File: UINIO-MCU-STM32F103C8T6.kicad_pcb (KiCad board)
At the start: 2 copper layers, 68.4 x 20.3 mm, 40 parts, among them J1 Conn_01x24_Pin, J2 Conn_01x24_Pin, J3 Conn_01x04_Pin, SW1 BOOT1, SW2 NRST, SW3 BOOT0, U1 ME6211C33M5G-N, U2 STM32F103C8T6, Y1 32.768KHz, Y2 8MHz

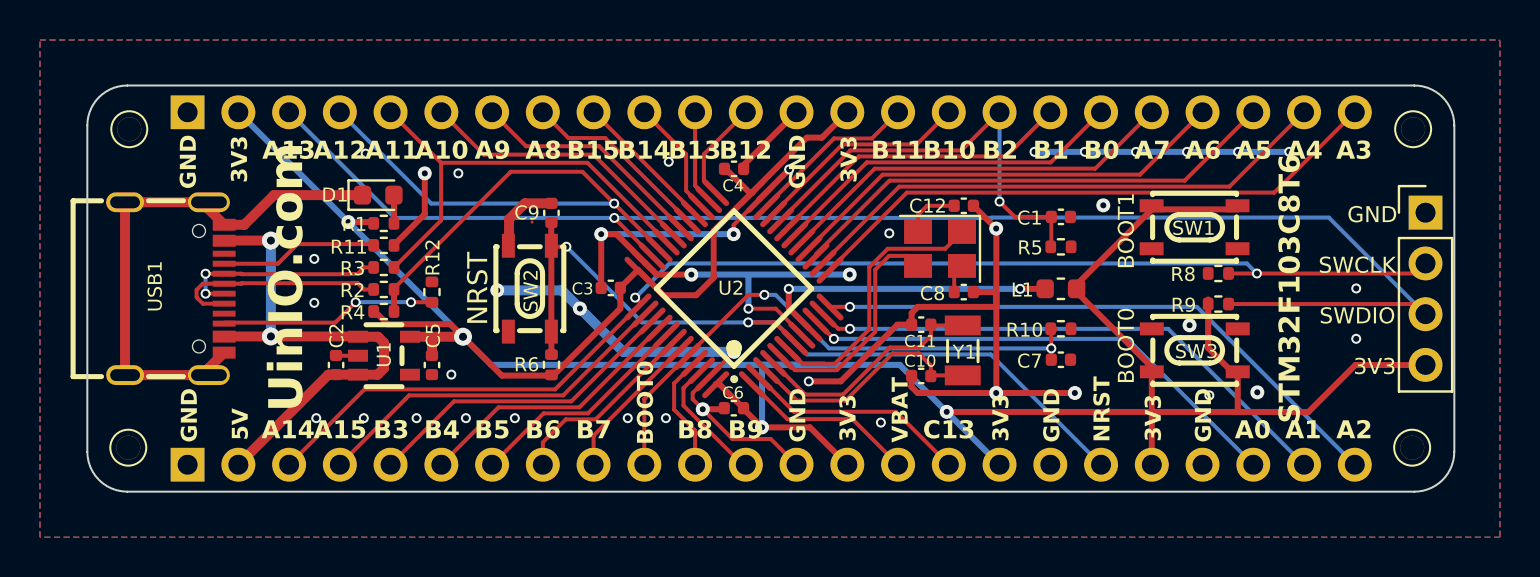
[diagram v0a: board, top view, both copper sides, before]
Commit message: Release UINIO-MCU-STM32F103C8T6 version 3.0.0.
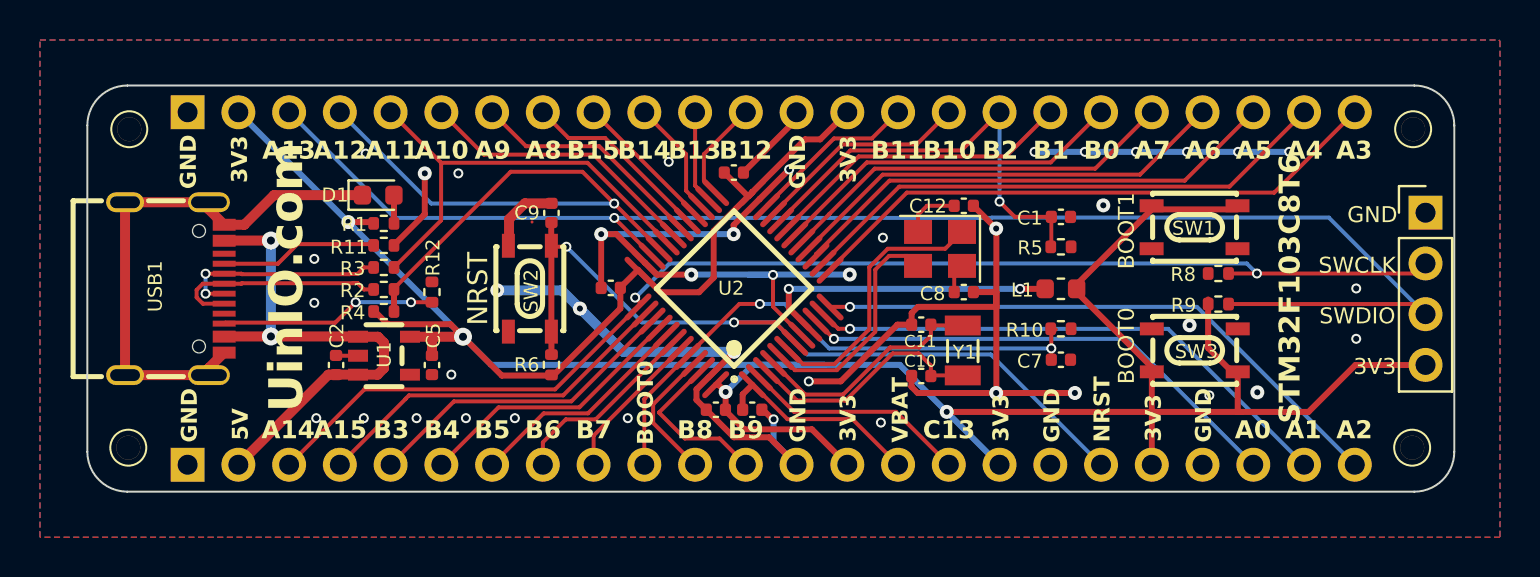
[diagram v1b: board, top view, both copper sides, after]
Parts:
- added C13: 0.1uF, Capacitor_SMD:C_0402_1005Metric, F.Cu at (150.6, 105.9)
- moved C6 0.90 mm to (148.8, 105.9)
- moved C4 0.19 mm to (149.7, 94.0)
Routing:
- net /PB9: track 6.34 -> 8.43 mm
- net GND: track 140.7 -> 142.8 mm, vias 42 -> 41
- net /VBAT: track 8.96 -> 10.4 mm
- net /PB8: track 5.95 -> 6.82 mm
- net /NRST: track 41.4 -> 42.1 mm

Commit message: update
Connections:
- L1 pad 1: /VDD_3.3V -> GND
- L1 pad 2: Net-(U2-VDDA) -> Net-(U2-VSSA)
- U2 pad 8: GND -> Net-(U2-VSSA)
- U2 pad 9: Net-(U2-VDDA) -> /VDD_3.3V
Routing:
- net Net-(U2-VSSA): track 0.00 -> 17.8 mm, vias 0 -> 2
- net Net-(U2-VDDA): track 15.5 -> 0.00 mm, vias 2 -> 0
- net /PA12: track 34.0 -> 26.7 mm
- net GND: track 142.8 -> 138.2 mm, vias 41 -> 53
- net /NRST: track 42.1 -> 41.2 mm
- net /VDD_3.3V: track 152.0 -> 152.9 mm
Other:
- board text added: "Version 3.1.0"
- board text removed: "Version 3.0.0"

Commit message: Release UINIO-MCU-STM32F103C8T6 version 3.2.0.
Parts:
- moved R12 0.54 mm to (134.7, 100.5), turned to 0 degrees
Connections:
- net /PA11 renamed /USB_PA11-
- net /PA12 renamed /USB_PA12+
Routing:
- net GND: track 138.2 -> 135.3 mm, vias 53 -> 55
- net /USB_PA11-: track 22.7 -> 24.7 mm, vias 0 -> 1
- net /NRST: track 41.2 -> 40.0 mm
- net /USB_PA12+: track 26.7 -> 27.7 mm
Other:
- board text added: "Version 3.2.0"
- board text removed: "Version 3.1.0"

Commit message: Release UINIO-MCU-STM32F103C8T6 version 3.2.0.
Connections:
- net /USB_PA11- renamed /USB_PA-
- net /USB_PA12+ renamed /USB_PA+
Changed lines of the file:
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@@
   (net 51 "Net-(USB1-CC2)")
   (net 52 "unconnected-(USB1-SBU2-PadB8)")
-  (net 53 "/USB_PA12+")
-  (net 54 "/USB_PA11-")
+  (net 53 "/USB_PA+")
+  (net 54 "/USB_PA-")
   (footprint "Resistor_SMD:R_0402_1005Metric" (layer "F.Cu")
     (at 132.14906 96.574468 180)
@@
       (net 4 "/VDD_3.3V") (pintype "passive"))
     (pad "2" smd roundrect (at 0.51 0) (size 0.54 0.64) (layers "F.Cu" "F.Paste" "F.Mask") (roundrect_rratio 0.25)
-      (net 53 "/USB_PA12+") (pintype "passive"))
+      (net 53 "/USB_PA+") (pintype "passive"))
     (model "${KICAD6_3DMODEL_DIR}/Resistor_SMD.3dshapes/R_0402_1005Metric.wrl"
       (offset (xyz 0 0 0))
@@
       (net 13 "/PA10") (pinfunction "PA10") (pintype "input"))
     (pad "32" smd oval (at -0.75 -4.05 45) (size 0.28 1.8) (layers "F.Cu" "F.Paste" "F.Mask")
-      (net 54 "/USB_PA11-") (pinfunction "PA11") (pintype "input"))
+      (net 54 "/USB_PA-") (pinfunction "PA11") (pintype "input"))
     (pad "33" smd oval (at -1.25 -4.05 45) (size 0.28 1.8) (layers "F.Cu" "F.Paste" "F.Mask")
-      (net 53 "/USB_PA12+") (pinfunction "PA12") (pintype "input"))
+      (net 53 "/USB_PA+") (pinfunction "PA12") (pintype "input"))
     (pad "34" smd oval (at -1.75 -4.05 45) (size 0.28 1.8) (layers "F.Cu" "F.Paste" "F.Mask")
       (net 12 "/PA13{slash}SWDIO") (pinfunction "PA13") (pintype "input"))
@@
       (net 45 "/USB_Data-") (pintype "passive"))
     (pad "2" smd roundrect (at 0.51 0) (size 0.54 0.64) (layers "F.Cu" "F.Paste" "F.Mask") (roundrect_rratio 0.25)
-      (net 54 "/USB_PA11-") (pintype "passive"))
+      (net 54 "/USB_PA-") (pintype "passive"))
     (model "${KICAD6_3DMODEL_DIR}/Resistor_SMD.3dshapes/R_0402_1005Metric.wrl"
       (offset (xyz 0 0 0))
@@
       (net 44 "/USB_Data+") (pintype "passive"))
     (pad "2" smd roundrect (at 0.51 0) (size 0.54 0.64) (layers "F.Cu" "F.Paste" "F.Mask") (roundrect_rratio 0.25)
-      (net 53 "/USB_PA12+") (pintype "passive"))
+      (net 53 "/USB_PA+") (pintype "passive"))
     (model "${KICAD6_3DMODEL_DIR}/Resistor_SMD.3dshapes/R_0402_1005Metric.wrl"
       (offset (xyz 0 0 0))
@@
       (net 12 "/PA13{slash}SWDIO") (pinfunction "Pin_3") (pintype "passive"))
     (pad "4" thru_hole oval (at 0 -7.62 270) (size 1.7 1.7) (drill 1) (layers "*.Cu" "*.Mask")
-      (net 53 "/USB_PA12+") (pinfunction "Pin_4") (pintype "passive"))
+      (net 53 "/USB_PA+") (pinfunction "Pin_4") (pintype "passive"))
     (pad "5" thru_hole oval (at 0 -10.16 270) (size 1.7 1.7) (drill 1) (layers "*.Cu" "*.Mask")
-      (net 54 "/USB_PA11-") (pinfunction "Pin_5") (pintype "passive"))
+      (net 54 "/USB_PA-") (pinfunction "Pin_5") (pintype "passive"))
     (pad "6" thru_hole oval (at 0 -12.7 270) (size 1.7 1.7) (drill 1) (layers "*.Cu" "*.Mask")
       (net 13 "/PA10") (pinfunction "Pin_6") (pintype "passive"))
@@
     )
   )
-  (zone (net 53) (net_name "/USB_PA12+") (layer "F.Cu") (name "$teardrop_padvia$") (hatch edge 0.5)
+  (zone (net 53) (net_name "/USB_PA+") (layer "F.Cu") (name "$teardrop_padvia$") (hatch edge 0.5)
     (priority 30162)
     (attr (teardrop (type padvia)))
@@
     )
   )
-  (zone (net 53) (net_name "/USB_PA12+") (layer "F.Cu") (name "$teardrop_padvia$") (hatch edge 0.5)
+  (zone (net 53) (net_name "/USB_PA+") (layer "F.Cu") (name "$teardrop_padvia$") (hatch edge 0.5)
     (priority 30139)
     (attr (teardrop (type padvia)))
@@
     )
   )
-  (zone (net 54) (net_name "/USB_PA11-") (layer "F.Cu") (name "$teardrop_padvia$") (hatch edge 0.5)
+  (zone (net 54) (net_name "/USB_PA-") (layer "F.Cu") (name "$teardrop_padvia$") (hatch edge 0.5)
     (priority 30137)
     (attr (teardrop (type padvia)))
@@
     )
   )
-  (zone (net 54) (net_name "/USB_PA11-") (layer "F.Cu") (name "$teardrop_padvia$") (hatch edge 0.5)
+  (zone (net 54) (net_name "/USB_PA-") (layer "F.Cu") (name "$teardrop_padvia$") (hatch edge 0.5)
     (priority 30160)
     (attr (teardrop (type padvia)))
@@
     )
   )
-  (zone (net 53) (net_name "/USB_PA12+") (layer "F.Cu") (name "$teardrop_padvia$") (hatch edge 0.5)
+  (zone (net 53) (net_name "/USB_PA+") (layer "F.Cu") (name "$teardrop_padvia$") (hatch edge 0.5)
     (priority 30087)
     (attr (teardrop (type padvia)))
@@
     )
   )
-  (zone (net 53) (net_name "/USB_PA12+") (layer "F.Cu") (name "$teardrop_padvia$") (hatch edge 0.5)
+  (zone (net 53) (net_name "/USB_PA+") (layer "F.Cu") (name "$teardrop_padvia$") (hatch edge 0.5)
     (priority 30086)
     (attr (teardrop (type padvia)))
@@
     )
   )
-  (zone (net 54) (net_name "/USB_PA11-") (layer "F.Cu") (name "$teardrop_padvia$") (hatch edge 0.5)
+  (zone (net 54) (net_name "/USB_PA-") (layer "F.Cu") (name "$teardrop_padvia$") (hatch edge 0.5)
     (priority 30155)
     (attr (teardrop (type padvia)))
@@
     )
   )
-  (zone (net 53) (net_name "/USB_PA12+") (layer "F.Cu") (name "$teardrop_padvia$") (hatch edge 0.5)
+  (zone (net 53) (net_name "/USB_PA+") (layer "F.Cu") (name "$teardrop_padvia$") (hatch edge 0.5)
     (priority 30163)
     (attr (teardrop (type padvia)))
@@
     )
   )
-  (zone (net 54) (net_name "/USB_PA11-") (layer "B.Cu") (name "$teardrop_padvia$") (hatch edge 0.5)
+  (zone (net 54) (net_name "/USB_PA-") (layer "B.Cu") (name "$teardrop_padvia$") (hatch edge 0.5)
     (priority 30003)
     (attr (teardrop (type padvia)))
@@
     )
   )
-  (zone (net 53) (net_name "/USB_PA12+") (layer "B.Cu") (name "$teardrop_padvia$") (hatch edge 0.5)
+  (zone (net 53) (net_name "/USB_PA+") (layer "B.Cu") (name "$teardrop_padvia$") (hatch edge 0.5)
     (priority 30005)
     (attr (teardrop (type padvia)))
@@
     )
   )
-  (zone (net 54) (net_name "/USB_PA11-") (layer "B.Cu") (name "$teardrop_padvia$") (hatch edge 0.5)
+  (zone (net 54) (net_name "/USB_PA-") (layer "B.Cu") (name "$teardrop_padvia$") (hatch edge 0.5)
     (priority 30024)
     (attr (teardrop (type padvia)))
@@
     )
   )
-  (zone (net 53) (net_name "/USB_PA12+") (layer "B.Cu") (name "$teardrop_padvia$") (hatch edge 0.5)
+  (zone (net 53) (net_name "/USB_PA+") (layer "B.Cu") (name "$teardrop_padvia$") (hatch edge 0.5)
     (priority 30025)
     (attr (teardrop (type padvia)))
